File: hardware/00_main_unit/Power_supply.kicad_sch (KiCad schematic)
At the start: 12 parts, among them IC1 MAX17503ATP+, IC4 TLV1117-33

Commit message: Fixes after wrong merge
Signed-off-by: Jacek <matuszewski.kartech@gmail.com>
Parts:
- C1: TME C0603C104K3RAC -> (none)
- C41: TME CL10A225KP8NNNC -> (none)
- C42: TME 0603B562K500CT -> (none)
- R52: TME CQ0603-180K-1% -> (none)
- R53: TME WF06P-39K-5% -> (none)
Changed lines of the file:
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@@
-      (effects (font (size 1.27 1.27)) hide)
-    )
-    (property "TME" "CQ0603-180K-1%" (id 4) (at 193.167 71.501 0)
       (effects (font (size 1.27 1.27)) hide)
     )
@@
     )
     (property "Datasheet" "~" (id 3) (at 193.167 82.931 0)
-      (effects (font (size 1.27 1.27)) hide)
-    )
-    (property "TME" "WF06P-39K-5%" (id 4) (at 193.167 82.931 0)
       (effects (font (size 1.27 1.27)) hide)
     )
@@
       (effects (font (size 1.27 1.27)) hide)
     )
-    (property "TME" "C0603C104K3RAC" (id 4) (at 140.335 67.31 0)
-      (effects (font (size 1.27 1.27)) hide)
-    )
     (pin "1")
     (pin "2")
@@
     )
     (property "Datasheet" "~" (id 3) (at 140.335 123.571 0)
-      (effects (font (size 1.27 1.27)) hide)
-    )
-    (property "TME" "0603B562K500CT" (id 4) (at 140.335 123.571 0)
       (effects (font (size 1.27 1.27)) hide)
     )
@@
       (effects (font (size 1.27 1.27)) hide)
     )
-    (property "TME" "CL10A225KP8NNNC" (id 4) (at 167.513 103.505 0)
-      (effects (font (size 1.27 1.27)) hide)
-    )

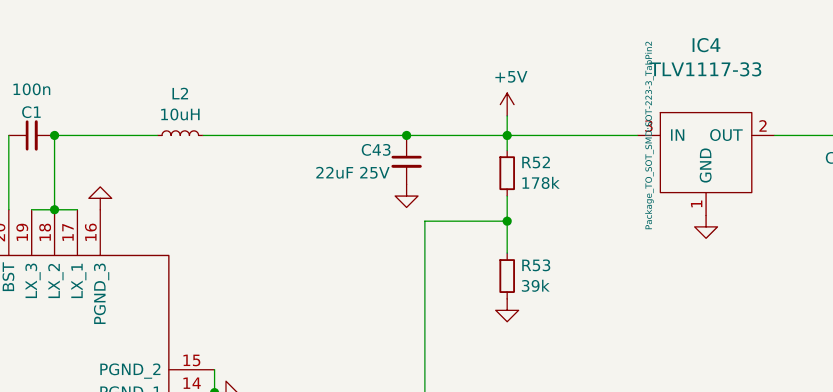
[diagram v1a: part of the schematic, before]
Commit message: Remote mode fixes
Signed-off-by: Jarosław Karwik <jaroslaw.karwik@gmail.com>
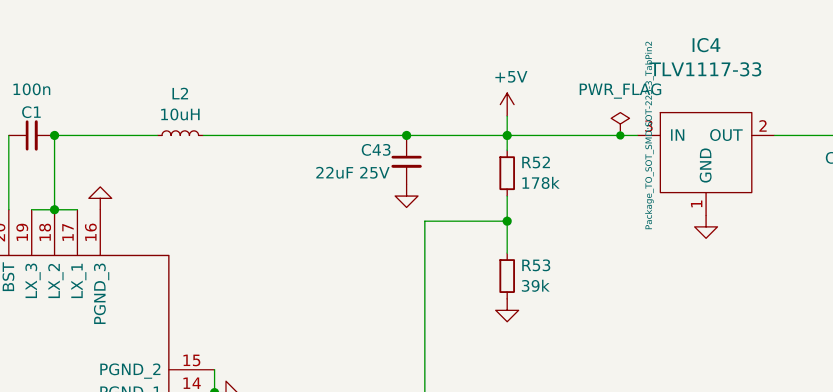
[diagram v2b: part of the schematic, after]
